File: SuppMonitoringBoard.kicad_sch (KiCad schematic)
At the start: 0 parts

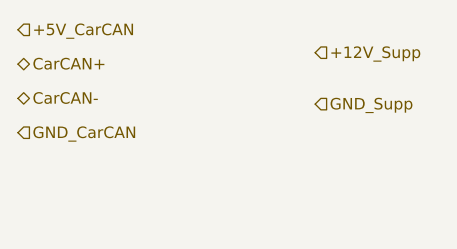
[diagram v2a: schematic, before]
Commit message: add LV pwr dist
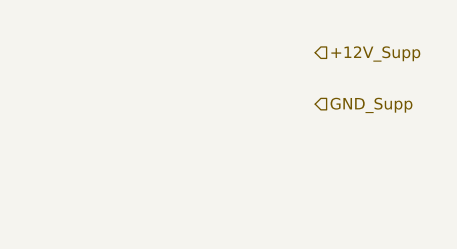
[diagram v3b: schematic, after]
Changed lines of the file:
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@@
 	(generator_version "9.0")
 	(paper "A4")
-	(hierarchical_label "GND_CarCAN"
-		(shape input)
-		(at 114.935 88.9 0)
-		(effects
-			(font
-				(size 1.27 1.27)
-			)
-			(justify left)
-		)
-	)
 	(hierarchical_label "+12V_Supp"
 		(shape input)
@@
 		(effects
 			(font
-				(size 1.27 1.27)
-			)
-			(justify left)
-		)
-	)
-	(hierarchical_label "+5V_CarCAN"
-		(shape input)
-		(at 114.935 77.47 0)
-		(effects
-			(font
-				(size 1.27 1.27)
-			)
-			(justify left)
-		)
-	)
-	(hierarchical_label "CarCAN+"
-		(shape bidirectional)
-		(at 114.935 81.28 0)
-		(effects
-			(font
-				(size 1.27 1.27)
-			)
-			(justify left)
-		)
-	)
-	(hierarchical_label "CarCAN-"
-		(shape bidirectional)
-		(at 114.935 85.09 0)
-		(effects
-			(font

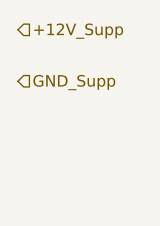
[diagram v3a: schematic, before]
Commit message: add suppmon shunt
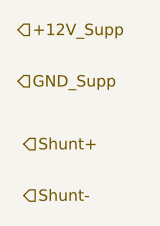
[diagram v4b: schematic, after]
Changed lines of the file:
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@@
 	(generator_version "9.0")
 	(paper "A4")
+	(hierarchical_label "Shunt-"
+		(shape input)
+		(at 148.59 98.425 0)
+		(effects
+			(font
+				(size 1.27 1.27)
+			)
+			(justify left)
+		)
+	)
+	(hierarchical_label "Shunt+"
+		(shape input)
+		(at 148.59 92.71 0)
+		(effects
+			(font
+				(size 1.27 1.27)
+			)
+			(justify left)
+		)
+	)
 	(hierarchical_label "+12V_Supp"
 		(shape input)
